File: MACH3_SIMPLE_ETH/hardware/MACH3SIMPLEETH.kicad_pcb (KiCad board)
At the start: 4 copper layers, 210 x 155 mm, 337 parts, among them J101 SENSORS / 24V IN, J201 USB-C, J202 SWD, J203 microSD, J301 HR911105A, J401 X axis, J402 Y axis, J403 Z axis, J404 A axis, J405 B axis, J406 C axis, J407 U axis, J408 V axis, J409 ENABLE, J501 LIMITS X Y Z A B C U V, J502 EST HLD RUN PRB, J503 THC AOK UP DN, J601 EXPANSION, J611 Relay A, J612 Relay B, J613 Relay C, J614 Relay D, J615 Relay E, J616 Relay F, J701 VFD, J801 RS485 A B GND, J802 HW ICSP, J803 MPG PENDANT, K601 JQC-3FF-024-1Z, K602 JQC-3FF-024-1Z, K603 JQC-3FF-024-1Z, K604 JQC-3FF-024-1Z, K605 JQC-3FF-024-1Z, K606 JQC-3FF-024-1Z, Q601 AO3400A, Q602 AO3400A, Q603 AO3400A, Q604 AO3400A, Q605 AO3400A, Q606 AO3400A, SW201 RESET, SW202 BOOTSEL, U101 LM2596S-5, U102 AP7361C-33E, U201 RP2350B, U202 W25Q128JVS, U203 USBLC6-2SC6, U301 W5500, U401 74ACT245, U402 74ACT245, U403 74ACT245, U501 PC847, U502 PC847, U503 PC847, U504 PC847, U601 MCP23017-E/SO, U701 74HCT14, U702 PC847, U703 B2412S-1WR3, U704 78L05, U705 LM358, U801 MAX3485ESA, U802 ATmega328P-AU, Y201 12MHz ABM8-272-T3, Y301 25MHz 18pF, Y801 8MHz

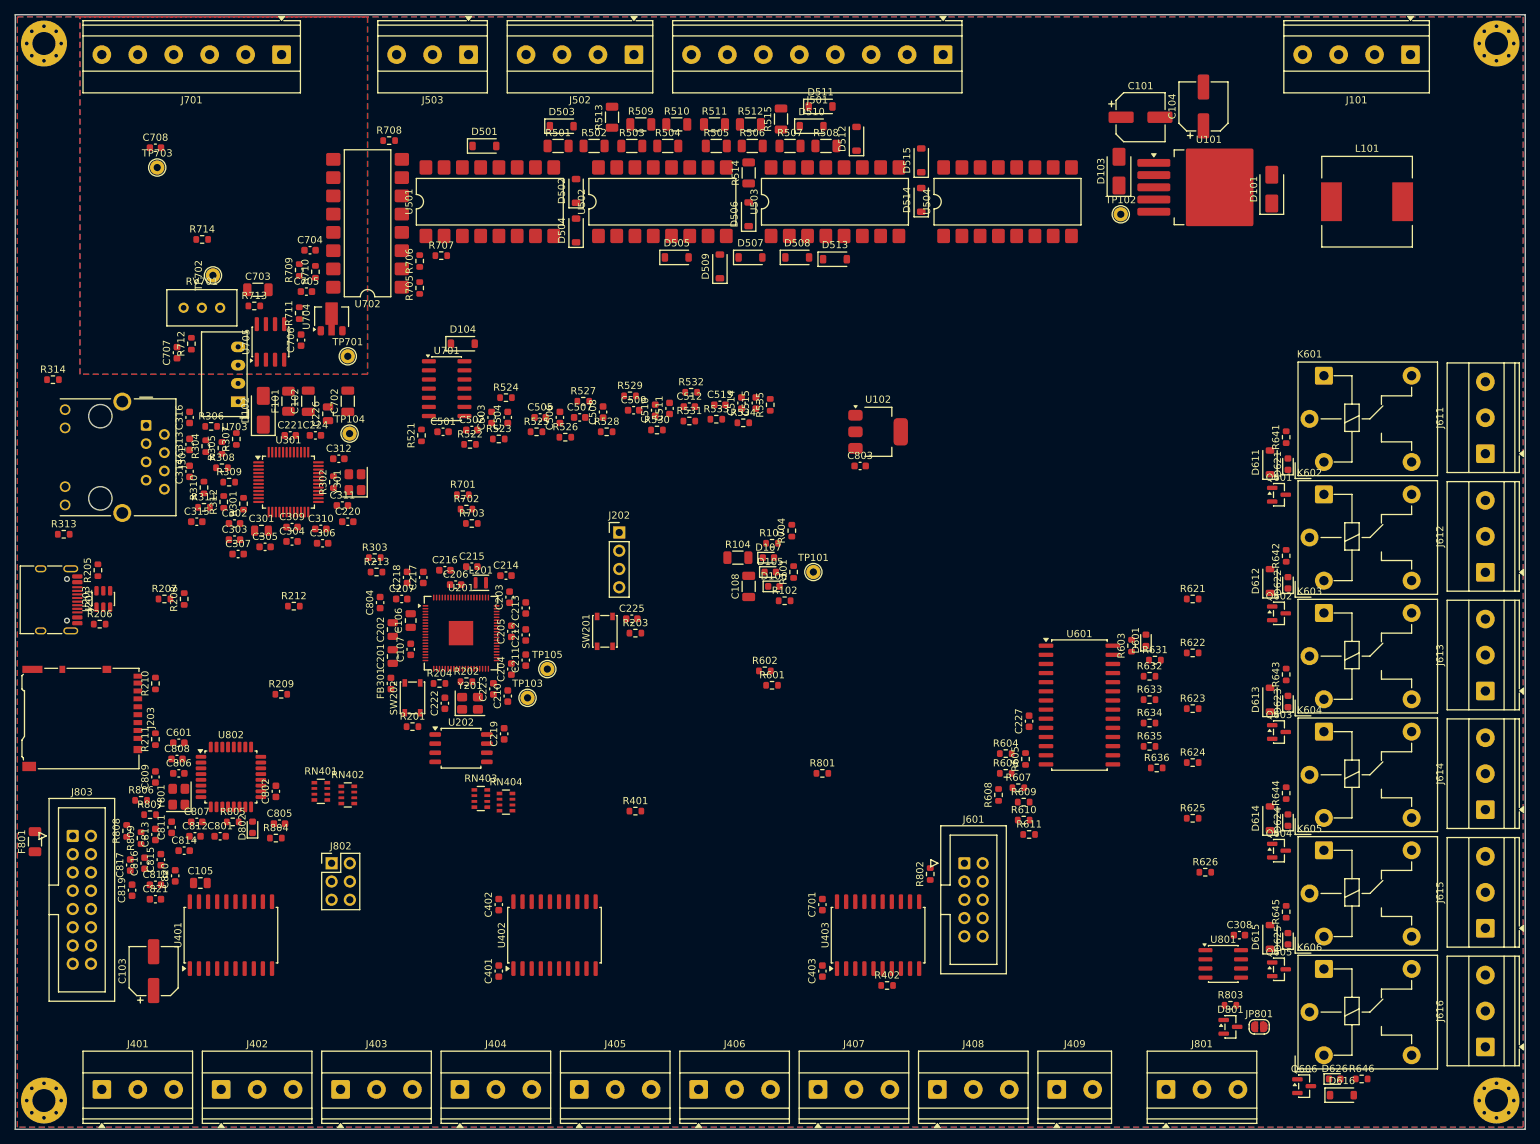
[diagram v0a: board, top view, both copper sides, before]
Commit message: MACH3-SIMPLE-ETH: bypass caps under the RP2350B/W5500 on the back, 2 mm clear ring
The previous route stalled at 110 unrouted: the auto-placer had put the
fine-pitch chips' bypass capacitors against their pins on the top, walling
in the GPIO. Those capacitors now go on the back under the chip, nothing
on the top comes within 2 mm of U201/U301, and the 24 V input chain is
fixed in line under J101.

Co-Authored-By: Claude Opus 5.5 <noreply@anthropic.com>
Claude-Session: https://claude.ai/code/session_01MByiLT2xCcbGPkgCYQy33q
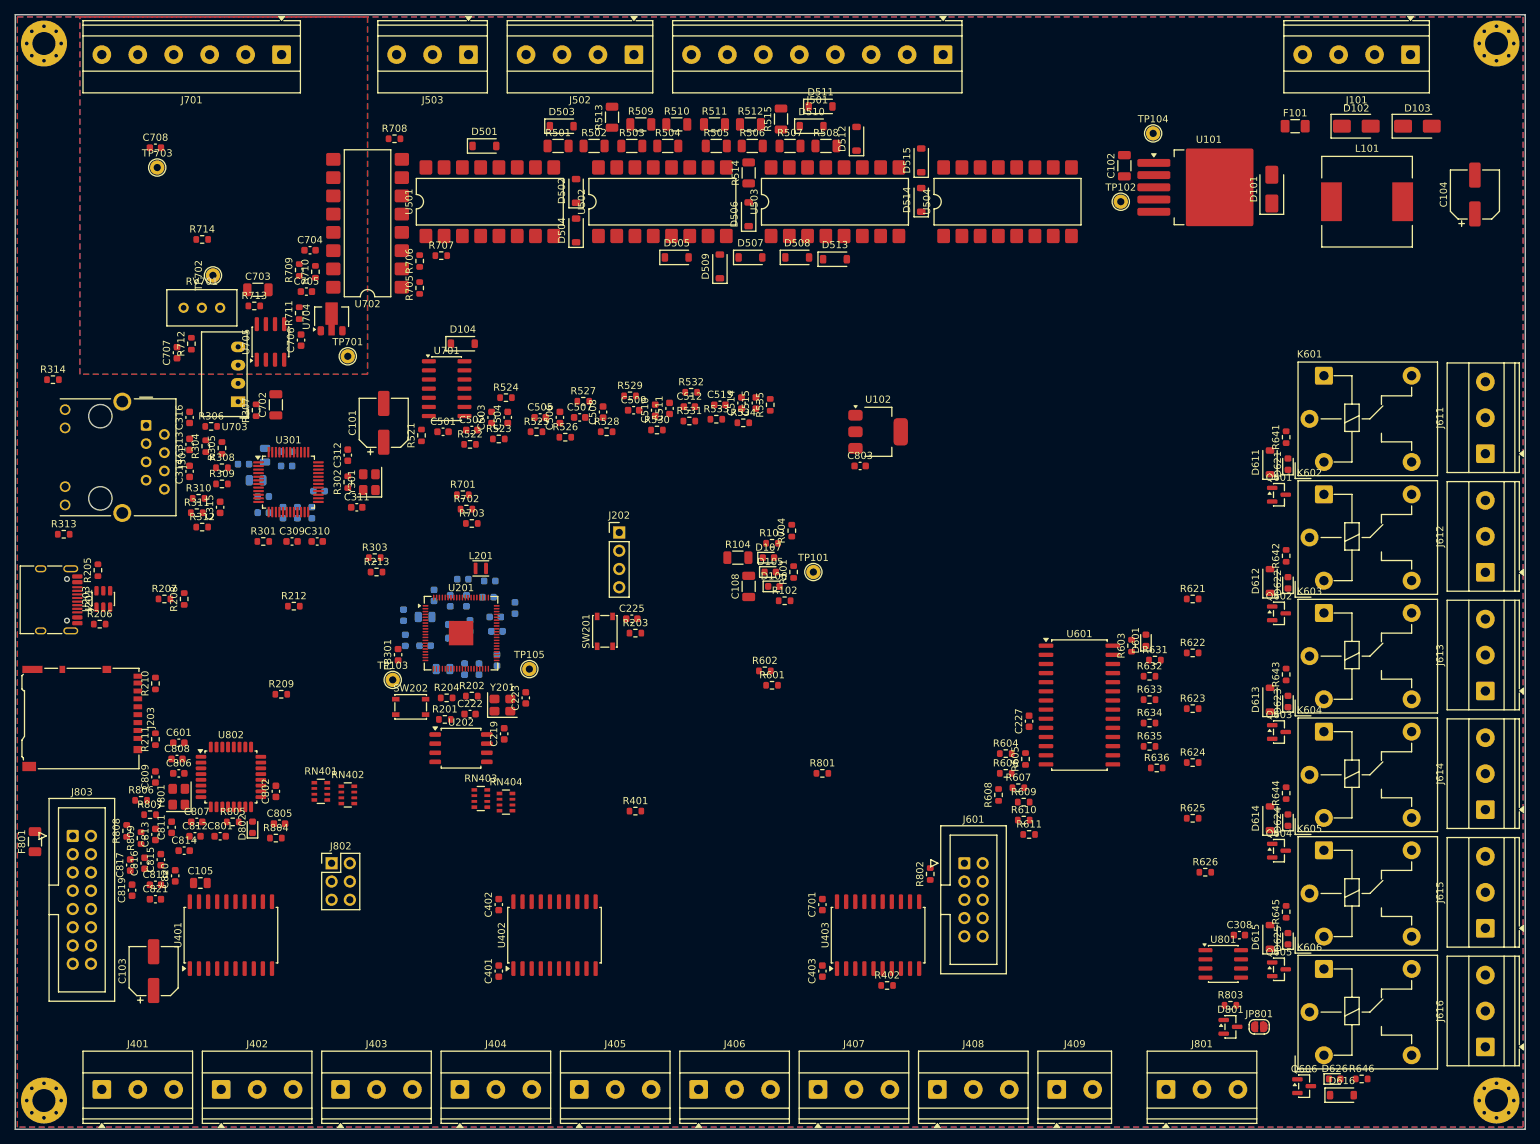
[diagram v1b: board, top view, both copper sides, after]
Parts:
- C106, C107, C201, C202, C203, C204, C205, C206, C207, C210, C211, C212, C213, C214, C215, C216, C217, C218, C220, C221, C224, C226, C301, C302, C303, C304, C305, C306, C307, C804: moved to B.Cu
- moved D102 157.0 mm to (186.5, 15.5), turned to 0 degrees
- moved F101 145.1 mm to (178.0, 15.5), turned to 0 degrees
- moved TP104 119.3 mm to (158.2, 16.5)
- moved C102 118.1 mm to (154.2, 21.0)
- moved C101 113.5 mm to (51.2, 56.8), turned to 90 degrees
- moved D103 42.0 mm to (195.0, 15.5), turned to 0 degrees
- moved C104 39.7 mm to (203.0, 25.0)
- moved TP103 18.9 mm to (52.5, 92.5)
- moved C307 12.5 mm to (31.8, 62.5)
- moved C226 10.5 mm to (34.8, 61.2)
- moved C702 10.0 mm to (36.2, 54.2)
- moved C217 9.37 mm to (63.2, 85.0)
- moved C202 8.00 mm to (60.5, 85.8)
- moved C201 7.22 mm to (59.5, 91.0), turned to 0 degrees
- moved C301 7.04 mm to (33.5, 64.8)
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
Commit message: MACH3-SIMPLE-ETH: routing pass 1 imported and filled
Freerouting pass 1 (board nets, VFD corner kept out): 1 h 40 min, 40
passes. After the zone fill 44 connections remain: 29 on the VFD side
(pass 2's job) and 15 others - 7 GND pins inside the RP2350B/W5500 fanout,
3 CHASSIS, 3 VBUS, 2 +3V3. Most of the 91 Freerouting reported were GND
pads that reach the ground pours once they are filled.

Co-Authored-By: Claude Opus 5.5 <noreply@anthropic.com>
Claude-Session: https://claude.ai/code/session_01MByiLT2xCcbGPkgCYQy33q
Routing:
- net +3V3: track 0.00 -> 693.7 mm, vias 0 -> 14
- net GND: track 0.00 -> 640.5 mm, vias 0 -> 3
- net V24: track 0.00 -> 482.2 mm, vias 0 -> 1
- net +5V: track 0.00 -> 452.5 mm, vias 0 -> 6
- net CHASSIS: track 0.00 -> 252.0 mm
- net NRST: track 0.00 -> 163.4 mm, vias 0 -> 7
- net RS485_DI: track 0.00 -> 155.4 mm, vias 0 -> 2
- net RS485_DE: track 0.00 -> 143.3 mm, vias 0 -> 2
- net RS485_RO: track 0.00 -> 143.2 mm, vias 0 -> 4
- net X_LIM: track 0.00 -> 112.0 mm, vias 0 -> 3
- net SP_AUX_IN: track 0.00 -> 107.7 mm, vias 0 -> 4
- net THC_DOWN: track 0.00 -> 105.7 mm, vias 0 -> 3
- net Y_LIM: track 0.00 -> 104.8 mm, vias 0 -> 4
- net THC_UP: track 0.00 -> 101.6 mm, vias 0 -> 4
- net ARC_OK: track 0.00 -> 101.0 mm, vias 0 -> 3
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
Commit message: MACH3-SIMPLE-ETH: bare mounting holes, VBUS/CHASSIS parts moved to their connectors
After pass 2, 16 connections were left. Three were CHASSIS between the
corner mounting holes, which needed a track round the whole board edge:
the holes are bare now, as on A1, and the shield bond is at the magjack and
USB. Three were VBUS, because the auto-placer had put D104 in the middle
of the board. tools/autoroute.py fixup brings the routed board up to the
regenerated schematic (paths, holes), moves D104/C108/R104 next to the pads
they serve, clears the tracks they now sit on, and adds In2 ground pours so
stitching vias can land in ground on every layer. Parity 0.

Co-Authored-By: Claude Opus 5.5 <noreply@anthropic.com>
Claude-Session: https://claude.ai/code/session_01MByiLT2xCcbGPkgCYQy33q
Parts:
- H101, H102, H103, H104: footprint MountingHole:MountingHole_3.2mm_M3_Pad_Via -> MountingHole:MountingHole_3.2mm_M3
- moved C108 102.1 mm to (4.75, 48.5), turned to 0 degrees
- moved R104 100.3 mm to (4.75, 45.8)
- moved D104 61.6 mm to (7.75, 74.5)
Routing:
- net CHASSIS: track 252.0 -> 0.00 mm
- net SP_12V: track 0.00 -> 50.1 mm, vias 0 -> 1
- net GND: track 640.5 -> 688.5 mm, vias 3 -> 4
- net SP_FWD: track 0.00 -> 36.5 mm, vias 0 -> 1
- net SP_DCM: track 0.00 -> 35.7 mm, vias 0 -> 1
- net SP_AVI: track 0.00 -> 35.0 mm
- net SP_REV: track 0.00 -> 32.4 mm, vias 0 -> 1
- net +3V3: track 693.7 -> 661.7 mm
- net SP_ACM: track 0.00 -> 31.3 mm
- net SP_OUT: track 0.00 -> 24.4 mm, vias 0 -> 2
- net SP_AUX: track 0.00 -> 22.2 mm
- net SP_5V: track 0.00 -> 17.0 mm, vias 0 -> 2
- net SP_F2: track 0.00 -> 15.8 mm
- net SP_F1: track 0.00 -> 10.8 mm
- net SP_FB: track 0.00 -> 6.27 mm
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- added copper zone on In2.Cu, net GND
- added copper zone on In2.Cu, net SP_ACM
